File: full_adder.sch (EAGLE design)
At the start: 75 parts, among them IC1 SN74LS74AN, IC2 NE555, IC3 CD4052BE, IC4 CD4052BE, IC5 CD4052BE, IC6 74HC4051N,652, U1 ATTINY45-20P

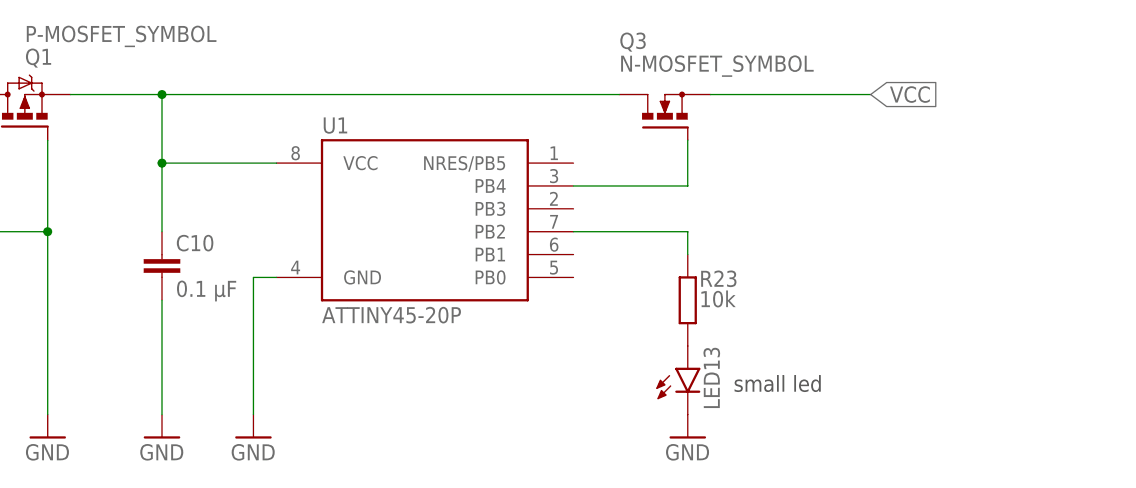
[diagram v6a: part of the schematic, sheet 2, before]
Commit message: fet pulldown
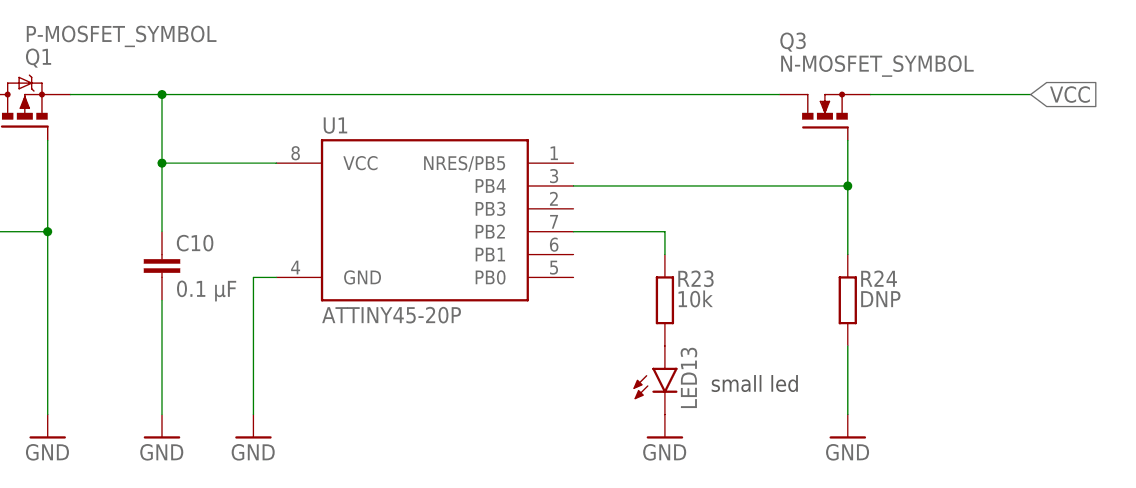
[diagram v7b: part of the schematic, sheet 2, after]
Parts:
- added R24: DNP, rcl:R-EU_R1206
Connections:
- net GND: now also R24.1
- net N$32: now also R24.2
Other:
- moved on the sheet: LED13, Q3, R23
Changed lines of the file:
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@@
 <part name="R23" library="rcl" library_urn="urn:adsk.eagle:library:334" deviceset="R-EU_" device="R1206" package3d_urn="urn:adsk.eagle:package:23540/2" value="10k"/>
 <part name="GND50" library="supply1" library_urn="urn:adsk.eagle:library:371" deviceset="GND" device=""/>
+<part name="R24" library="rcl" library_urn="urn:adsk.eagle:library:334" deviceset="R-EU_" device="R1206" package3d_urn="urn:adsk.eagle:package:23540/2" value="DNP"/>
+<part name="GND51" library="supply1" library_urn="urn:adsk.eagle:library:371" deviceset="GND" device=""/>
 </parts>
 <sheets>
@@
 <plain>
 <text x="-177.8" y="190.5" size="3.81" layer="100">10 Reverse Polarity + Overdischarge Protection</text>
-<text x="-73.66" y="144.78" size="1.778" layer="97">small led</text>
+<text x="-76.2" y="144.78" size="1.778" layer="97">small led</text>
 </plain>
 <instances>
@@
 <attribute name="VALUE" x="-139.7" y="137.16" size="1.778" layer="96"/>
 </instance>
-<instance part="Q3" gate="G$1" x="-81.28" y="175.26" smashed="yes" rot="R90">
-<attribute name="NAME" x="-86.36" y="182.88" size="1.778" layer="95"/>
-<attribute name="VALUE" x="-86.36" y="180.34" size="1.778" layer="96"/>
-</instance>
-<instance part="LED13" gate="G$1" x="-78.74" y="147.32" smashed="yes">
-<attribute name="NAME" x="-75.184" y="142.748" size="1.778" layer="95" rot="R90"/>
-<attribute name="VALUE" x="-73.025" y="142.748" size="1.778" layer="96" rot="R90"/>
-</instance>
-<instance part="R23" gate="G$1" x="-78.74" y="154.94" smashed="yes" rot="R90">
-<attribute name="NAME" x="-77.47" y="156.4386" size="1.778" layer="95"/>
-<attribute name="VALUE" x="-77.47" y="154.178" size="1.778" layer="96"/>
-</instance>
-<instance part="GND50" gate="1" x="-78.74" y="139.7" smashed="yes">
-<attribute name="VALUE" x="-81.28" y="137.16" size="1.778" layer="96"/>
+<instance part="Q3" gate="G$1" x="-63.5" y="175.26" smashed="yes" rot="R90">
+<attribute name="NAME" x="-68.58" y="182.88" size="1.778" layer="95"/>
+<attribute name="VALUE" x="-68.58" y="180.34" size="1.778" layer="96"/>
+</instance>
+<instance part="LED13" gate="G$1" x="-81.28" y="147.32" smashed="yes">
+<attribute name="NAME" x="-77.724" y="142.748" size="1.778" layer="95" rot="R90"/>
+<attribute name="VALUE" x="-75.565" y="142.748" size="1.778" layer="96" rot="R90"/>
+</instance>
+<instance part="R23" gate="G$1" x="-81.28" y="154.94" smashed="yes" rot="R90">
+<attribute name="NAME" x="-80.01" y="156.4386" size="1.778" layer="95"/>
+<attribute name="VALUE" x="-80.01" y="154.178" size="1.778" layer="96"/>
+</instance>
+<instance part="GND50" gate="1" x="-81.28" y="139.7" smashed="yes">
+<attribute name="VALUE" x="-83.82" y="137.16" size="1.778" layer="96"/>
+</instance>
+<instance part="R24" gate="G$1" x="-60.96" y="154.94" smashed="yes" rot="R90">
+<attribute name="NAME" x="-59.69" y="156.4386" size="1.778" layer="95"/>
+<attribute name="VALUE" x="-59.69" y="154.178" size="1.778" layer="96"/>
+</instance>
+<instance part="GND51" gate="1" x="-60.96" y="139.7" smashed="yes">
+<attribute name="VALUE" x="-63.5" y="137.16" size="1.778" layer="96"/>
 </instance>
 </instances>
@@
 <pinref part="LED13" gate="G$1" pin="C"/>
 </segment>
+<segment>
+<pinref part="R24" gate="G$1" pin="1"/>
+<pinref part="GND51" gate="1" pin="GND"/>
+<wire x1="-60.96" y1="149.86" x2="-60.96" y2="142.24" width="0.1524" layer="91"/>
+</segment>
 </net>
 <net name="N$31" class="0">
@@
 <wire x1="-137.16" y1="177.8" x2="-137.16" y2="170.18" width="0.1524" layer="91"/>
 <wire x1="-137.16" y1="170.18" x2="-124.46" y2="170.18" width="0.1524" layer="91"/>
-<wire x1="-137.16" y1="177.8" x2="-86.36" y2="177.8" width="0.1524" layer="91"/>
+<wire x1="-137.16" y1="177.8" x2="-68.58" y2="177.8" width="0.1524" layer="91"/>
 <junction x="-137.16" y="177.8"/>
 <pinref part="C10" gate="G$1" pin="1"/>
@@
 <net name="VCC" class="0">
 <segment>
-<wire x1="-76.2" y1="177.8" x2="-58.42" y2="177.8" width="0.1524" layer="91"/>
-<label x="-58.42" y="177.8" size="1.778" layer="95" xref="yes"/>
+<wire x1="-58.42" y1="177.8" x2="-40.64" y2="177.8" width="0.1524" layer="91"/>
+<label x="-40.64" y="177.8" size="1.778" layer="95" xref="yes"/>
 </segment>
 </net>
@@
 <segment>
 <pinref part="U1" gate="G$1" pin="PB4"/>
-<wire x1="-91.44" y1="167.64" x2="-78.74" y2="167.64" width="0.1524" layer="91"/>
-<wire x1="-78.74" y1="167.64" x2="-78.74" y2="172.72" width="0.1524" layer="91"/>
+<wire x1="-91.44" y1="167.64" x2="-60.96" y2="167.64" width="0.1524" layer="91"/>
+<wire x1="-60.96" y1="167.64" x2="-60.96" y2="172.72" width="0.1524" layer="91"/>
+<pinref part="R24" gate="G$1" pin="2"/>
+<wire x1="-60.96" y1="167.64" x2="-60.96" y2="160.02" width="0.1524" layer="91"/>
+<junction x="-60.96" y="167.64"/>
 </segment>
 </net>
@@
 <segment>
 <pinref part="U1" gate="G$1" pin="PB2"/>
-<wire x1="-91.44" y1="162.56" x2="-78.74" y2="162.56" width="0.1524" layer="91"/>
+<wire x1="-91.44" y1="162.56" x2="-81.28" y2="162.56" width="0.1524" layer="91"/>
 <pinref part="R23" gate="G$1" pin="2"/>
-<wire x1="-78.74" y1="162.56" x2="-78.74" y2="160.02" width="0.1524" layer="91"/>
-</segment>
-</net>
+<wire x1="-81.28" y1="162.56" x2="-81.28" y2="160.02" width="0.1524" layer="91"/>
+</segment>
+</net>

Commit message: finalization + cleanup
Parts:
- removed C1: 0.01 µF, rcl:C-EU025-024X044
- removed C10, C3, C4, C8: 0.1 µF, rcl:C-EU025-024X044
- removed C2: 1 µF, rcl:C-EU025-024X044
- removed GND_IN, VCC_IN: LSP11, solpad:LSP11
- removed IC1: SN74LS74AN, SN74LS74AN:SN74LS74AN
- removed IC2: NE555, st-microelectronics_555_timer:NE555
- removed LED1, LED10, LED11, LED12, LED13, LED2, LED3, LED4, LED5, LED6, LED7, LED8, LED9: (no value), led:LED5MM
- removed R1, R17, R18, R19, R2, R20: 1k, rcl:R-EU_R1206
- removed R10, R11, R12, R13, R14, R15, R4, R5, R6, R7, R8, R9: 2k2, rcl:R-EU_R1206
- removed R23: 10k, rcl:R-EU_R1206
- removed R24: DNP, rcl:R-EU_R1206
- removed R3: 1M, custom:POTENTIOMETER
- removed S1: KM28C65A-20, custom:KM28C65A-20
- removed U$1, U$2, U$3, U$4, U$5, U$6, U$7, U$8: TOGGLESWITCH, custom:TOGGLESWITCH
- removed U1: ATTINY45-20P, _hhn_attiny25_45_85:ATTINY45-20P
- added C101, C301, C302, C303, C304, C305, C401, C603, C701: 0.1 µF, rcl:C-EU025-024X044
- added C601: 1 µF, rcl:C-EU025-024X044
- added C602: 0.01 µF, rcl:C-EU025-024X044
- added GND_IN1, VCC_IN1: LSP11, solpad:LSP11
- added LED1001, LED1002, LED1003, LED1004, LED1005, LED101, LED1101, LED1102, LED1103, LED1104, LED1105, LED1106, LED1107, LED1108: (no value), led:LED5MM
- added R1001, R1002, R1003, R1004, R1005, R1101, R1102, R1103, R1104, R1105, R1106, R1107, R1108: 2k2, rcl:R-EU_R1206
- added R101: 10k, rcl:R-EU_R1206
- added R102: DNP, rcl:R-EU_R1206
- added R401, R402, R406, R407, R601, R602: 1k, rcl:R-EU_R1206
- added R603: 1M, custom:POTENTIOMETER
- added S901, S902, S903, S904, S905, S906, S907, S908: TOGGLESWITCH, custom:TOGGLESWITCH
- added U1001, U1002, U1003: FDS6892A, SamacSys_Parts:FDS6892A
- added U101: ATTINY45-20P, _hhn_attiny25_45_85:ATTINY45-20P
- added U401: KM28C65A-20, custom:KM28C65A-20
- added U601: NE555, st-microelectronics_555_timer:NE555
- added U701: SN74LS74AN, SN74LS74AN:SN74LS74AN
- renumbered AND_1 to AND_301, AND_2 to AND_302, C5 to C501, C6 to C202, C7 to C203, C9 to C201, IC3 to U201, IC4 to U202, IC5 to U203, IC6 to U501, OR_1 to OR_301, R16 to R403, R21 to R404, R22 to R405, XOR_1 to XOR_301, XOR_2 to XOR_302
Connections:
- removed net N$30: VCC_IN.MP
- removed net N$31: C10.1, U1.VCC
- removed net N$32: R24.2, U1.PB4
- removed net N$33: LED13.A, R23.1
- removed net N$34: R23.2, U1.PB2
- new net N$35: LED1005.A, R1005.1
- new net N$36: LED1001.C, U1001.D1, U1001.D1_1
- new net N$37: LED1002.C, U1001.D2, U1001.D2_1
- new net N$38: LED1003.C, U1002.D1, U1002.D1_1
- new net N$39: LED1005.C, U1003.D1, U1003.D1_1
- new net N$40: LED1004.C, U1002.D2, U1002.D2_1
- new net N$41: VCC_IN1.MP
- new net N$42: C101.1, U101.VCC
- new net N$43: R102.2, U101.PB4
- new net N$44: LED101.A, R101.1
- new net N$45: R101.2, U101.PB2
- net A0: now also R1101.2, S901.P$X; no longer R4.2, U$1.P$X
- net A1: now also R1102.2, S902.P$X; no longer R5.2, U$2.P$X
- net A2: now also R1103.2, S903.P$X; no longer R6.2, U$3.P$X
- net A3: now also R1104.2, S904.P$X; no longer R7.2, U$4.P$X
- net B0: now also R1105.2, S905.P$X; no longer R8.2, U$5.P$X
- net B1: now also R1106.2, S906.P$X; no longer R9.2, U$6.P$X
- net B2: now also R1107.2, S907.P$X; no longer R10.2, U$7.P$X
- net B3: now also R1108.2, S908.P$X; no longer R11.2, U$8.P$X
- net BCD_DATA_A: now also R401.1, R401.2, U401.I/O0; no longer R403.1, R403.2, S1.I/O0
- net BCD_DATA_B: now also R402.1, R402.2, U401.I/O1; no longer R17.1, R17.2, S1.I/O1
- net BCD_DATA_C: now also R403.1, R403.2, U401.I/O2; no longer R18.1, R18.2, S1.I/O2
- net BCD_DATA_D: now also R404.1, R404.2, U401.I/O3; no longer R19.1, R19.2, S1.I/O3
- net BCD_DATA_E: now also R405.1, R405.2, U401.I/O4; no longer R20.1, R20.2, S1.I/O4
- net BCD_DATA_F: now also R406.1, R406.2, U401.I/O5; no longer R404.1, R404.2, S1.I/O5
- net BCD_DATA_G: now also R407.1, R407.2, U401.I/O6; no longer R405.1, R405.2, S1.I/O6
- net C1: now also U701.1!Q, U701.1D, U701.1Q, U701.2CLK; no longer IC1.1!Q, IC1.1D, IC1.1Q, IC1.2CLK
- net C2: now also U701.2Q; no longer IC1.2Q
- net CLK: now also U401.A5, U601.OUT, U701.1CLK; no longer IC1.1CLK, IC2.OUT, S1.A5
- net COUT_3: now also U1003.G1
- net DISP_DATA_0: now also U401.A0; no longer S1.A0
- net DISP_DATA_1: now also U401.A1; no longer S1.A1
- net DISP_DATA_2: now also U401.A2; no longer S1.A2
- net DISP_DATA_3: now also U401.A3; no longer S1.A3
- net DISP_DATA_4: now also U401.A4; no longer S1.A4
- net GND: now also C101.2, C301.2, C302.2, C303.2, C304.2, C305.2, C401.2, C601.2, C602.2, C603.2, C701.2, GND_IN1.MP, LED101.C, LED1101.C, LED1102.C, LED1103.C, LED1104.C, LED1105.C, LED1106.C, LED1107.C, LED1108.C, R102.1, S901.P$A, S902.P$A, S903.P$A, S904.P$A, S905.P$A, S906.P$A, S907.P$A, S908.P$A, U1001.S1, U1001.S2, U1002.S1, U1002.S2, U1003.S1, U101.GND, U401.!CE, U401.!OE, U401.A10, U401.A11, U401.A12, U401.A6, U401.A7, U401.A8, U401.A9, U401.GND, U601.GND, U701.GND; no longer C1.2, C10.2, C2.2, C3.2, C4.2, C8.2, GND_IN.MP, IC1.GND, IC2.GND, LED1.C, LED10.C, LED11.C, LED12.C, LED13.C, LED2.C, LED3.C, LED4.C, LED5.C, LED6.C, LED7.C, LED8.C, LED9.C, R24.1, S1.!CE, S1.!OE, S1.A10, S1.A11, S1.A12, S1.A6, S1.A7, S1.A8, S1.A9, S1.GND, U$1.P$A, U$2.P$A, U$3.P$A, U$4.P$A, U$5.P$A, U$6.P$A, U$7.P$A, U$8.P$A, U1.GND
- net N$11: now also C602.1, U601.CON; no longer C1.1, IC2.CON
- net N$14: now also C601.1, R603.P$2, U601.TRE, U601.TRI; no longer C2.1, IC2.TRE, IC2.TRI, R3.P$2
- net N$15: now also R602.1, R603.P$1; no longer R2.1, R3.P$1
- net N$16: now also R601.1, R602.2, U601.DIS; no longer IC2.DIS, R1.1, R2.2
- net N$17: now also U701.2!Q, U701.2D; no longer IC1.2!Q, IC1.2D
- net N$18: now also LED1101.A, R1101.1; no longer LED1.A, R4.1
- net N$19: now also LED1102.A, R1102.1; no longer LED2.A, R5.1
- net N$20: now also LED1103.A, R1103.1; no longer LED3.A, R6.1
- net N$21: now also LED1104.A, R1104.1; no longer LED4.A, R7.1
- net N$22: now also LED1105.A, R1105.1; no longer LED5.A, R8.1
- net N$23: now also LED1106.A, R1106.1; no longer LED6.A, R9.1
- net N$24: now also LED1107.A, R1107.1; no longer LED7.A, R10.1
- net N$25: now also LED1108.A, R1108.1; no longer LED8.A, R11.1
- net N$26: now also LED1001.A, R1001.1; no longer LED9.A, R12.1
- net N$27: now also LED1002.A, R1002.1; no longer LED10.A, R13.1
- net N$28: now also LED1003.A, R1003.1; no longer LED11.A, R14.1
- net N$29: now also LED1004.A, R1004.1; no longer LED12.A, R15.1
- net S0: now also U1001.G1; no longer R12.2
- net S1: now also U1001.G2; no longer R13.2
- net S2: now also U1002.G1; no longer R14.2
- net S3: now also U1002.G2; no longer R15.2
- net VCC: now also C301.1, C302.1, C303.1, C304.1, C305.1, C401.1, C603.1, C701.1, R1001.2, R1002.2, R1003.2, R1004.2, R1005.2, R601.2, S901.P$B, S902.P$B, S903.P$B, S904.P$B, S905.P$B, S906.P$B, S907.P$B, S908.P$B, U401.!WE, U401.VCC, U601./RES, U601.VCC+, U701.1!CLR, U701.1!PRE, U701.2!CLR, U701.2!PRE, U701.VCC; no longer C3.1, C4.1, C8.1, IC1.1!CLR, IC1.1!PRE, IC1.2!CLR, IC1.2!PRE, IC1.VCC, IC2./RES, IC2.VCC+, R1.2, S1.!WE, S1.VCC, U$1.P$B, U$2.P$B, U$3.P$B, U$4.P$B, U$5.P$B, U$6.P$B, U$7.P$B, U$8.P$B
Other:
- note added: "1 Reverse Polarity + Overdischarge Protection"
- note added: "10 Binary Output LEDs"
- note added: "11 Binary Input LEDs"
- note added: "2 Input MUX"
- note added: "3 Adder"
- note added: "4 EEPROM (bcd decoder)"
- note added: "5 Output MUX"
- note added: "6 Clock"
- note added: "7 counter"
- note added: "8 7-segment displays"
- note added: "9 Input Selection"
- note removed: "1 clock"
- note removed: "10 Reverse Polarity + Overdischarge Protection"
- note removed: "2 counter"
- note removed: "3 input MUX"
- note removed: "4 Adder"
- note removed: "5 EEPROM (bcd decoder)"
- note removed: "6 output MUX"
- note removed: "7 input selection"
- note removed: "8 binary outputs"
- note removed: "9 7-segment displays"
- note removed: "transistor array fehlt"
